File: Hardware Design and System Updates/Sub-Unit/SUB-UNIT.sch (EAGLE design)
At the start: 10 parts, among them U1 MSP430FR2000IPW16PW16_TEX, U2 TLR342F-GE2SOP8_ROM, U4 TMP36GT9ZT_3_ADI

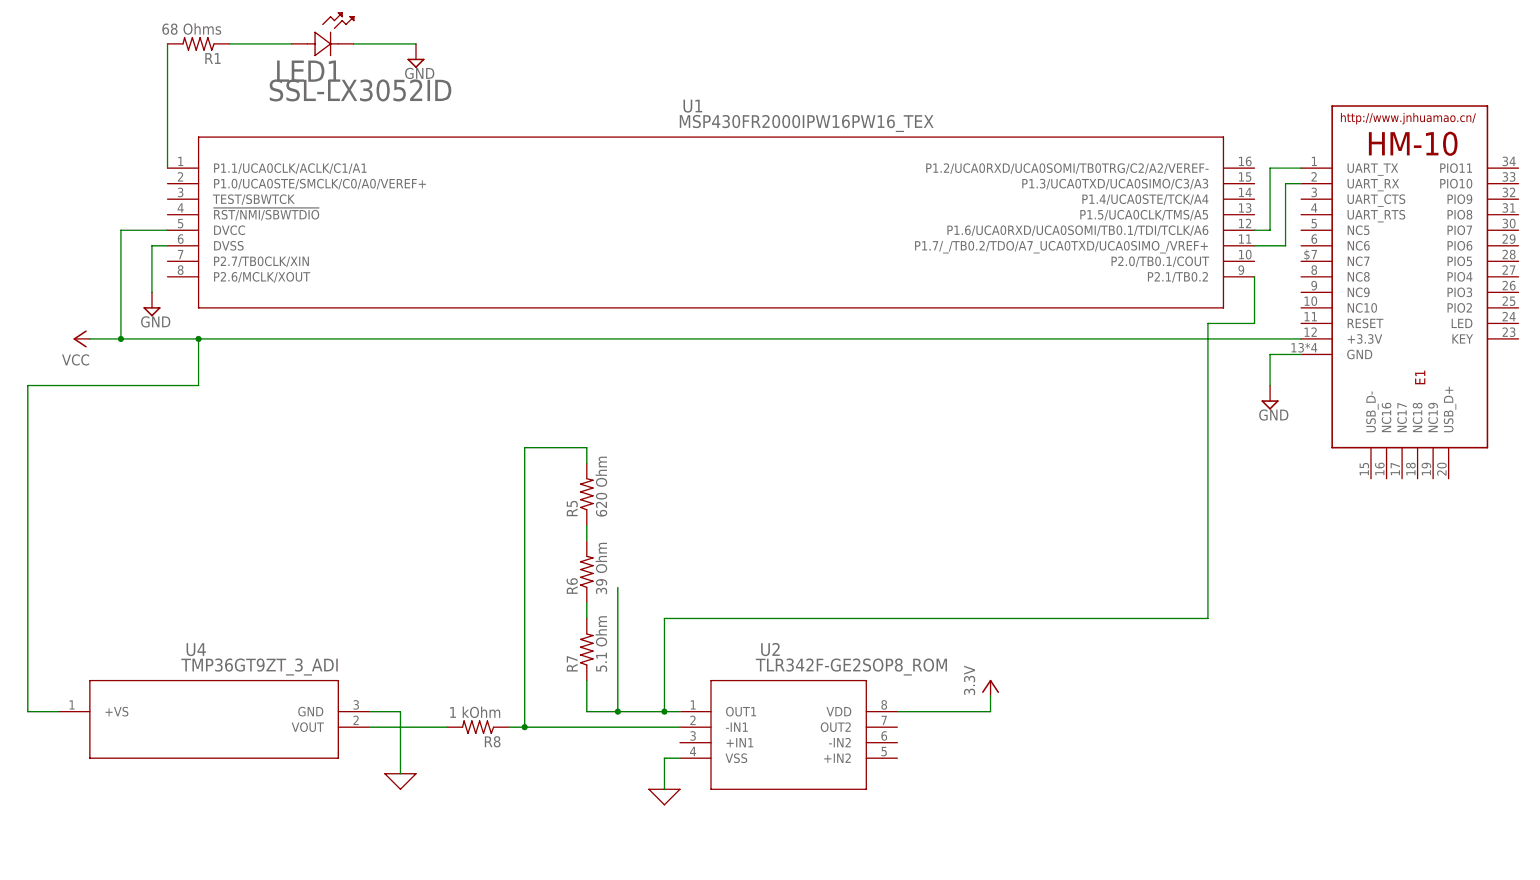
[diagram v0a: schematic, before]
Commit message: Added 5v regulator to schematics
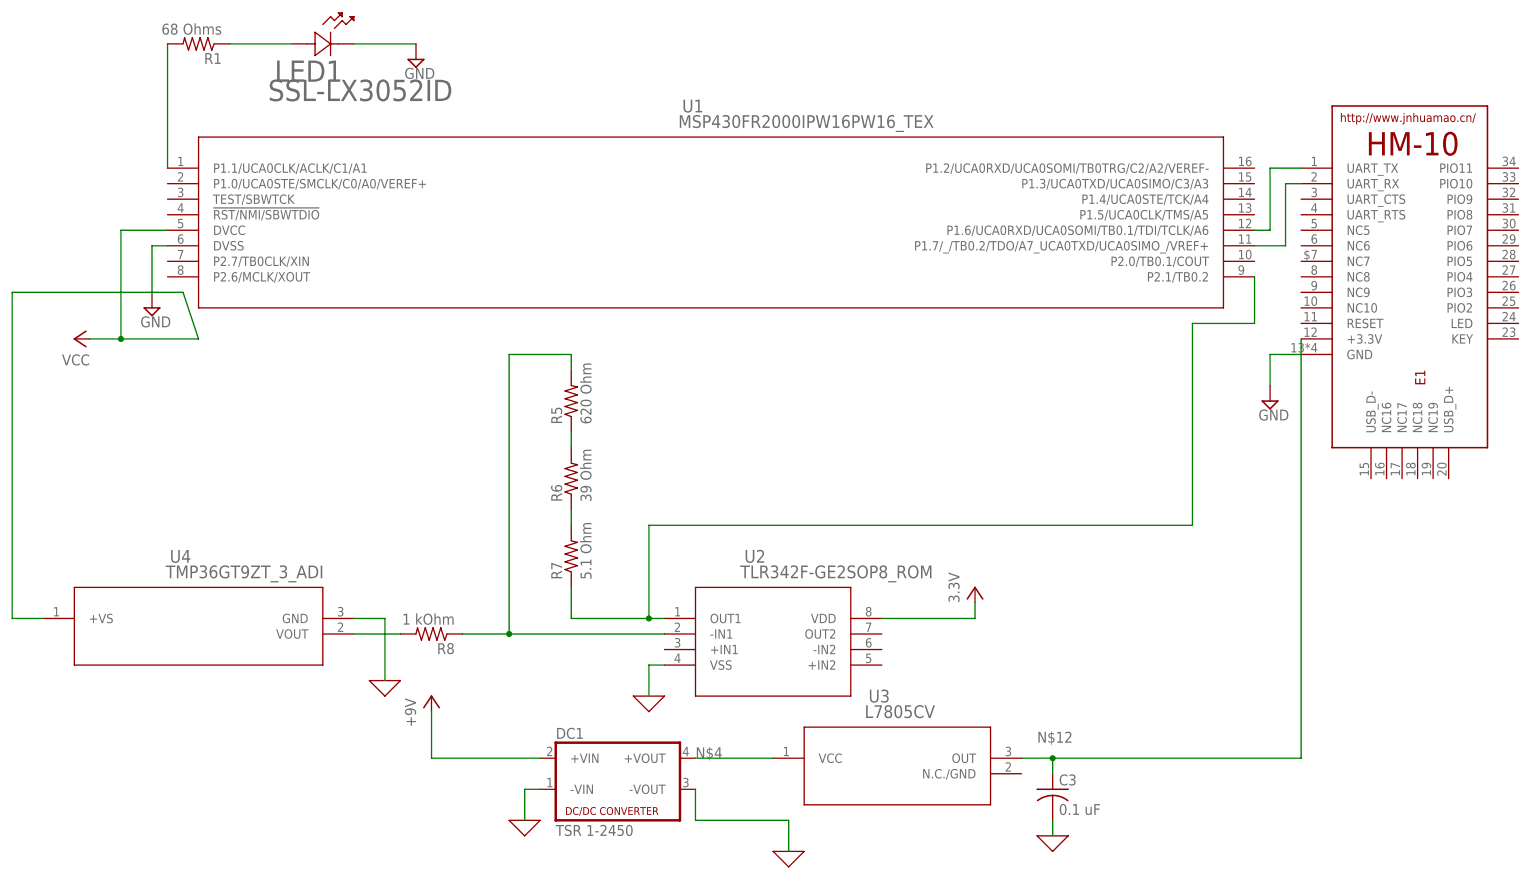
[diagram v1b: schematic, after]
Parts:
- added C3: 0.1 uF, rcl:C-US050-024X044
- added DC1: TSR 1-2450, dc-dc-converter:NME
- added U3: L7805CV, 2023-03-08_12-17-23_Library:BA033CC0FP-E2TO252-3_ROM
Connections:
- new net +5V: DC1.+VIN
- net 0: now also C3.2, DC1.-VIN, DC1.-VOUT
- net N$12: now also C3.1, E1.+3.3V, U3.OUT
- net N$4: now also DC1.+VOUT, U3.VCC
- net VCC: no longer E1.+3.3V
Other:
- moved on the sheet: R5, R6, R7, R8, U2, U4

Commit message: Fixed system schematics
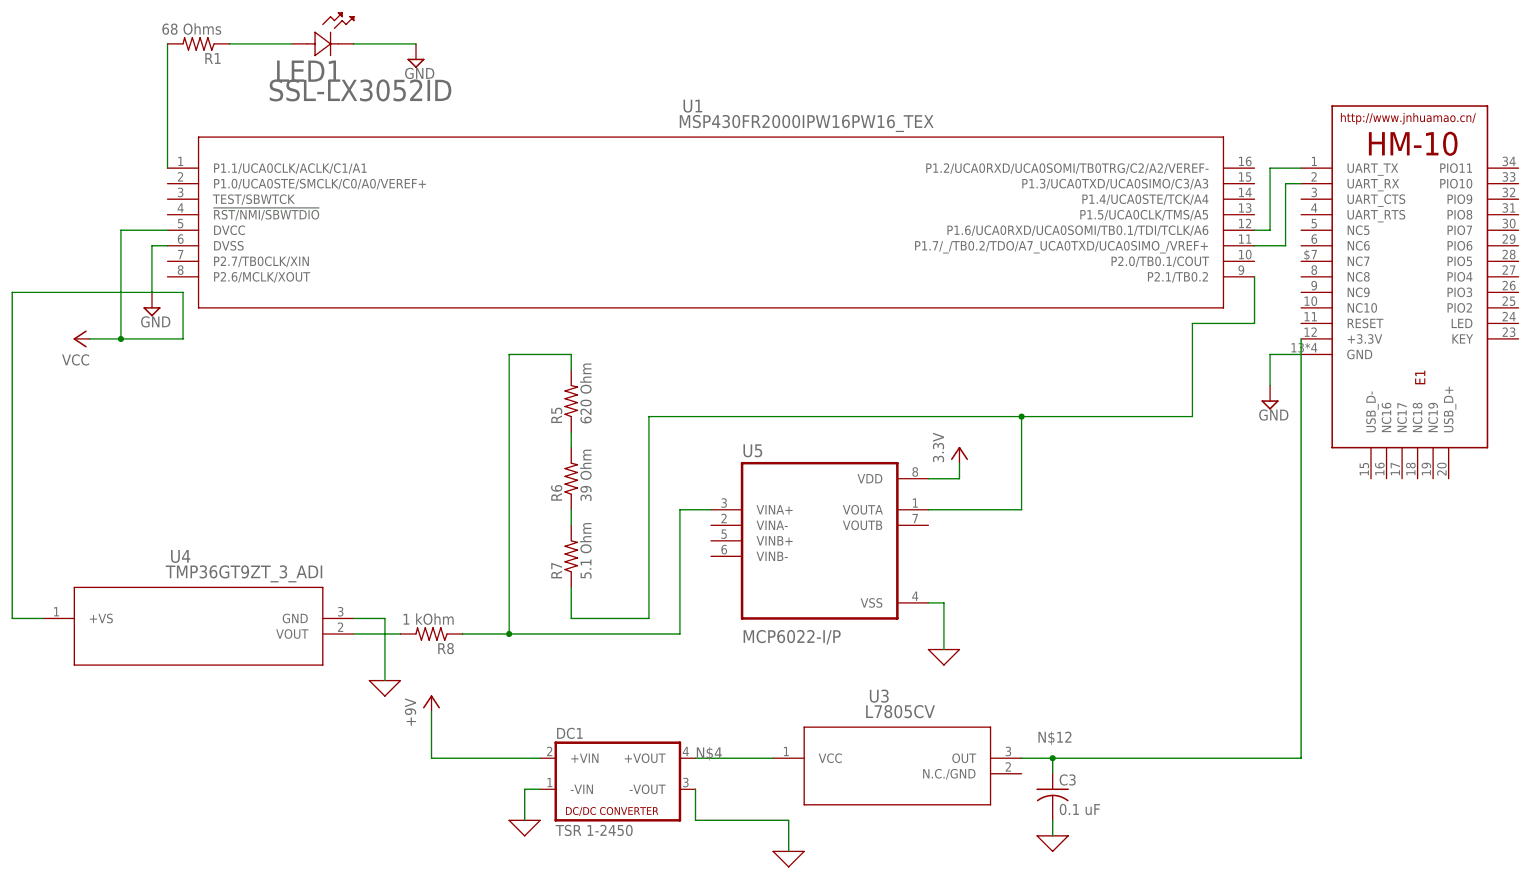
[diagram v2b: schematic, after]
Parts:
- removed U2: TLR342F-GE2SOP8_ROM, 2023-03-28_11-48-47_Library:TLR342F-GE2SOP8_ROM
- added U5: MCP6022-I/P, MCP6022-I_P:MCP6022-I/P
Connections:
- net 0: now also U5.VSS; no longer U2.VSS
- net N$12: now also U5.VINA+; no longer U2.-IN1
- net N$5: now also U5.VOUTA; no longer U2.OUT1
- net VCC: now also U5.VDD; no longer U2.VDD
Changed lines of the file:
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@@
 <part name="SUPPLY3" library="supply2" library_urn="urn:adsk.eagle:library:372" deviceset="GND" device=""/>
 <part name="P+1" library="supply1" library_urn="urn:adsk.eagle:library:371" deviceset="VCC" device=""/>
-<part name="U2" library="2023-03-28_11-48-47_Library" deviceset="TLR342F-GE2" device="SOP8_ROM"/>
 <part name="P+2" library="supply1" library_urn="urn:adsk.eagle:library:371" deviceset="VCC" device="" value="3.3V"/>
 <part name="X_5" library="ngspice-simulation" library_urn="urn:adsk.eagle:library:527439" deviceset="GND" device=""/>
@@
 <part name="X_10" library="ngspice-simulation" library_urn="urn:adsk.eagle:library:527439" deviceset="GND" device=""/>
 <part name="P+3" library="supply1" library_urn="urn:adsk.eagle:library:371" deviceset="+5V" device="" value="+9V"/>
+<part name="U5" library="MCP6022-I_P" deviceset="MCP6022-I/P" device=""/>
 </parts>
 <sheets>
@@
 <attribute name="VALUE" x="-312.42" y="91.44" size="1.778" layer="96" rot="R180"/>
 </instance>
-<instance part="U2" gate="A" x="-220.98" y="48.26" smashed="yes">
-<attribute name="NAME" x="-205.3854" y="57.3786" size="2.083" layer="95" ratio="6"/>
-<attribute name="VALUE" x="-206.0248" y="54.8386" size="2.083" layer="96" ratio="6"/>
-</instance>
-<instance part="P+2" gate="VCC" x="-167.64" y="53.34" smashed="yes">
-<attribute name="VALUE" x="-170.18" y="50.8" size="1.778" layer="96" rot="R90"/>
-</instance>
-<instance part="X_5" gate="G$1" x="-220.98" y="35.56" smashed="yes"/>
+<instance part="P+2" gate="VCC" x="-170.18" y="76.2" smashed="yes">
+<attribute name="VALUE" x="-172.72" y="73.66" size="1.778" layer="96" rot="R90"/>
+</instance>
+<instance part="X_5" gate="G$1" x="-172.72" y="43.18" smashed="yes"/>
 <instance part="R5" gate="G$1" x="-233.68" y="83.82" smashed="yes" rot="R90">
 <attribute name="NAME" x="-235.1786" y="80.01" size="1.778" layer="95" rot="R90"/>
@@
 <instance part="P+3" gate="1" x="-256.54" y="35.56" smashed="yes">
 <attribute name="VALUE" x="-259.08" y="30.48" size="1.778" layer="96" rot="R90"/>
+</instance>
+<instance part="U5" gate="A" x="-193.04" y="60.96" smashed="yes">
+<attribute name="NAME" x="-205.74" y="74.66" size="2.0828" layer="95" ratio="10" rot="SR0"/>
+<attribute name="VALUE" x="-205.74" y="44.26" size="2.0828" layer="96" ratio="10" rot="SR0"/>
 </instance>
 </instances>
@@
 <net name="VCC" class="0">
 <segment>
+<pinref part="P+1" gate="VCC" pin="VCC"/>
+<wire x1="-307.34" y1="93.98" x2="-297.18" y2="93.98" width="0.1524" layer="91"/>
+<junction x="-307.34" y="93.98"/>
+<wire x1="-307.34" y1="93.98" x2="-312.42" y2="93.98" width="0.1524" layer="91"/>
+<wire x1="-307.34" y1="111.76" x2="-307.34" y2="93.98" width="0.1524" layer="91"/>
 <pinref part="U1" gate="A" pin="DVCC"/>
 <wire x1="-299.72" y1="111.76" x2="-307.34" y2="111.76" width="0.1524" layer="91"/>
-<wire x1="-307.34" y1="111.76" x2="-307.34" y2="93.98" width="0.1524" layer="91"/>
-<wire x1="-307.34" y1="93.98" x2="-294.64" y2="93.98" width="0.1524" layer="91"/>
-<junction x="-307.34" y="93.98"/>
-<wire x1="-307.34" y1="93.98" x2="-312.42" y2="93.98" width="0.1524" layer="91"/>
-<pinref part="P+1" gate="VCC" pin="VCC"/>
 <pinref part="U4" gate="A" pin="+VS"/>
 <wire x1="-320.04" y1="48.26" x2="-325.12" y2="48.26" width="0.1524" layer="91"/>
 <wire x1="-325.12" y1="48.26" x2="-325.12" y2="101.6" width="0.1524" layer="91"/>
 <wire x1="-325.12" y1="101.6" x2="-297.18" y2="101.6" width="0.1524" layer="91"/>
-<wire x1="-297.18" y1="101.6" x2="-294.64" y2="93.98" width="0.1524" layer="91"/>
-</segment>
-<segment>
-<pinref part="U2" gate="A" pin="VDD"/>
-<wire x1="-182.88" y1="48.26" x2="-167.64" y2="48.26" width="0.1524" layer="91"/>
+<wire x1="-297.18" y1="101.6" x2="-297.18" y2="93.98" width="0.1524" layer="91"/>
+</segment>
+<segment>
+<pinref part="U5" gate="A" pin="VDD"/>
+<wire x1="-175.26" y1="71.12" x2="-170.18" y2="71.12" width="0.1524" layer="91"/>
 <pinref part="P+2" gate="VCC" pin="VCC"/>
-<wire x1="-167.64" y1="48.26" x2="-167.64" y2="50.8" width="0.1524" layer="91"/>
+<wire x1="-170.18" y1="71.12" x2="-170.18" y2="73.66" width="0.1524" layer="91"/>
 </segment>
 </net>
 <net name="0" class="0">
-<segment>
-<pinref part="X_5" gate="G$1" pin="0"/>
-<pinref part="U2" gate="A" pin="VSS"/>
-<wire x1="-220.98" y1="35.56" x2="-220.98" y2="40.64" width="0.1524" layer="91"/>
-<wire x1="-220.98" y1="40.64" x2="-218.44" y2="40.64" width="0.1524" layer="91"/>
-</segment>
 <segment>
 <pinref part="U4" gate="A" pin="GND"/>
@@
 <wire x1="-154.94" y1="12.7" x2="-154.94" y2="15.24" width="0.1524" layer="91"/>
 </segment>
+<segment>
+<pinref part="U5" gate="A" pin="VSS"/>
+<wire x1="-175.26" y1="50.8" x2="-172.72" y2="50.8" width="0.1524" layer="91"/>
+<pinref part="X_5" gate="G$1" pin="0"/>
+<wire x1="-172.72" y1="50.8" x2="-172.72" y2="43.18" width="0.1524" layer="91"/>
+</segment>
 </net>
 <net name="N$9" class="0">
@@
 <wire x1="-233.68" y1="88.9" x2="-233.68" y2="91.44" width="0.1524" layer="91"/>
 <wire x1="-233.68" y1="91.44" x2="-243.84" y2="91.44" width="0.1524" layer="91"/>
-<pinref part="U2" gate="A" pin="-IN1"/>
-<wire x1="-218.44" y1="45.72" x2="-243.84" y2="45.72" width="0.1524" layer="91"/>
 <wire x1="-243.84" y1="91.44" x2="-243.84" y2="45.72" width="0.1524" layer="91"/>
 <pinref part="R8" gate="G$1" pin="1"/>
 <wire x1="-251.46" y1="45.72" x2="-243.84" y2="45.72" width="0.1524" layer="91"/>
+<wire x1="-243.84" y1="45.72" x2="-215.9" y2="45.72" width="0.1524" layer="91"/>
 <junction x="-243.84" y="45.72"/>
+<pinref part="U5" gate="A" pin="VINA+"/>
+<wire x1="-215.9" y1="45.72" x2="-215.9" y2="66.04" width="0.1524" layer="91"/>
+<wire x1="-215.9" y1="66.04" x2="-210.82" y2="66.04" width="0.1524" layer="91"/>
 </segment>
 <segment>
@@
 <pinref part="R7" gate="G$1" pin="1"/>
 <wire x1="-233.68" y1="48.26" x2="-233.68" y2="53.34" width="0.1524" layer="91"/>
-<pinref part="U2" gate="A" pin="OUT1"/>
-<wire x1="-218.44" y1="48.26" x2="-220.98" y2="48.26" width="0.1524" layer="91"/>
 <wire x1="-220.98" y1="48.26" x2="-233.68" y2="48.26" width="0.1524" layer="91"/>
-<junction x="-220.98" y="48.26"/>
-<wire x1="-220.98" y1="63.5" x2="-220.98" y2="48.26" width="0.1524" layer="91"/>
+<wire x1="-220.98" y1="81.28" x2="-220.98" y2="48.26" width="0.1524" layer="91"/>
 <pinref part="U1" gate="A" pin="P2.1/TB0.2"/>
 <wire x1="-121.92" y1="104.14" x2="-121.92" y2="96.52" width="0.1524" layer="91"/>
 <wire x1="-121.92" y1="96.52" x2="-132.08" y2="96.52" width="0.1524" layer="91"/>
-<wire x1="-132.08" y1="96.52" x2="-132.08" y2="63.5" width="0.1524" layer="91"/>
-<wire x1="-220.98" y1="63.5" x2="-132.08" y2="63.5" width="0.1524" layer="91"/>
-</segment>
-</net>
+<wire x1="-132.08" y1="96.52" x2="-132.08" y2="81.28" width="0.1524" layer="91"/>
+<wire x1="-220.98" y1="81.28" x2="-160.02" y2="81.28" width="0.1524" layer="91"/>
+<pinref part="U5" gate="A" pin="VOUTA"/>
+<wire x1="-160.02" y1="81.28" x2="-132.08" y2="81.28" width="0.1524" layer="91"/>
+<wire x1="-175.26" y1="66.04" x2="-160.02" y2="66.04" width="0.1524" layer="91"/>
+<wire x1="-160.02" y1="66.04" x2="-160.02" y2="81.28" width="0.1524" layer="91"/>
+<junction x="-160.02" y="81.28"/>
+</segment>
+</net>
